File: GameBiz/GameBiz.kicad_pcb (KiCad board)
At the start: 2 copper layers, 89 x 51 mm, 90 parts, among them J1 USB4155-03-C_REVA, M1 C0720B001F, Q1 PMCXB900UEZ, SW1 CUS-12TB, U1 W25Q128JV, U2 RP2040, U3 NCV8718BMT330TBG, U4 BQ25172DSGR, U5 74LVC1G3157FZ4-7, U6 NRF24L01, U7 IQS7222A001QNR, U8 TPS61291DRVT, U9 EADOGS104NA, Y1 12MHz, Y2 ECS-160-18-30B-JEM-TR

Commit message: layout almost finished
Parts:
- removed TH1: Thermistor, Resistor_SMD:R_0603_1608Metric
- added R12: 10K, Resistor_SMD:R_0603_1608Metric, F.Cu at (159.9, 139.8)
- moved C19 118.0 mm to (131.4, 141.5)
- moved R21 117.4 mm to (176.4, 144.1), turned to -90 degrees
- moved Y2 116.0 mm to (179.2, 142.7), turned to -90 degrees
- moved SW1 115.4 mm to (140.8, 152.1)
- moved R13 115.2 mm to (118.2, 150.3)
- moved L3 115.2 mm to (191.9, 144.4), turned to -90 degrees
- moved D3 114.7 mm to (161.5, 141.6), turned to -90 degrees
- moved U4 109.8 mm to (157.7, 139.8), turned to 90 degrees
- moved U3 108.3 mm to (158.2, 144.9), turned to -90 degrees
- moved C15 107.3 mm to (156.4, 143.0), turned to -90 degrees
- moved R7 106.3 mm to (158.8, 142.2)
- moved U6 105.8 mm to (183.9, 142.4)
- moved R16 105.6 mm to (111.9, 143.0)
- moved C10 105.0 mm to (151.9, 128.1), turned to -90 degrees
- moved D2 104.7 mm to (145.0, 136.1), turned to -90 degrees
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- renumbered R12 to R13, R13 to R14, R14 to R15, R15 to R16, R16 to R17, R17 to R18, R18 to R19, R19 to R20, R20 to R21
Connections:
- AE1 pad 1: GND -> Net-(AE1-Pad2)
- AE1 pad 2: Net-(AE1-Pad2) -> GND
- D2 pad 1: unconnected-(D2-Pad1) -> Net-(D1-Pad1)
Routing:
- net Net-(BT1-Pad2): track 0.00 -> 180.5 mm, vias 0 -> 1
- net +3.3V: track 0.00 -> 94.4 mm
- net GND: track 0.00 -> 66.3 mm
- net Net-(C13-Pad2): track 0.00 -> 31.8 mm
- net Net-(C12-Pad2): track 0.00 -> 26.4 mm
- net Net-(BT1-Pad1): track 0.00 -> 26.1 mm, vias 0 -> 2
- net Net-(SW1-Pad2): track 0.00 -> 25.9 mm
- net Net-(J1-PadA6): track 0.00 -> 25.0 mm, vias 0 -> 2
- net Net-(R3-Pad1): track 0.00 -> 24.8 mm
- net Net-(C22-Pad2): track 0.00 -> 20.9 mm
- net Net-(Q1-Pad2): track 0.00 -> 19.9 mm
- net Net-(U1-Pad7): track 0.00 -> 19.5 mm
- net Net-(U1-Pad6): track 0.00 -> 17.2 mm
- net Net-(J1-PadA7): track 0.00 -> 16.6 mm, vias 0 -> 2
- net Net-(U1-Pad5): track 0.00 -> 14.0 mm
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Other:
- outline, holes or cut-outs redrawn

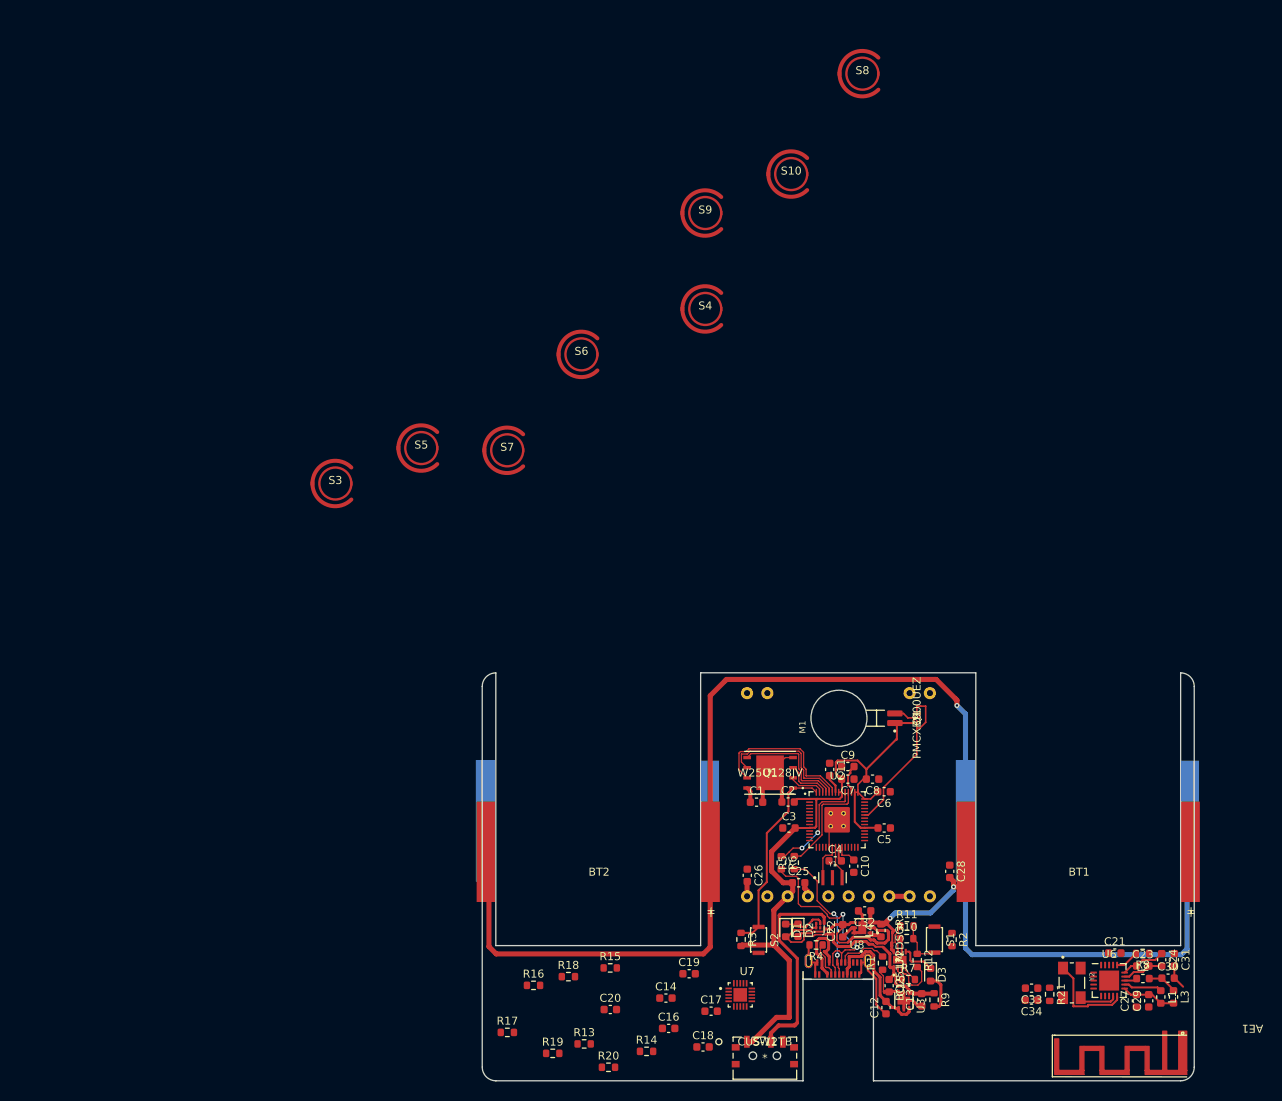
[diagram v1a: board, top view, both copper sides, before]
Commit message: capacitive buttons need to be finished
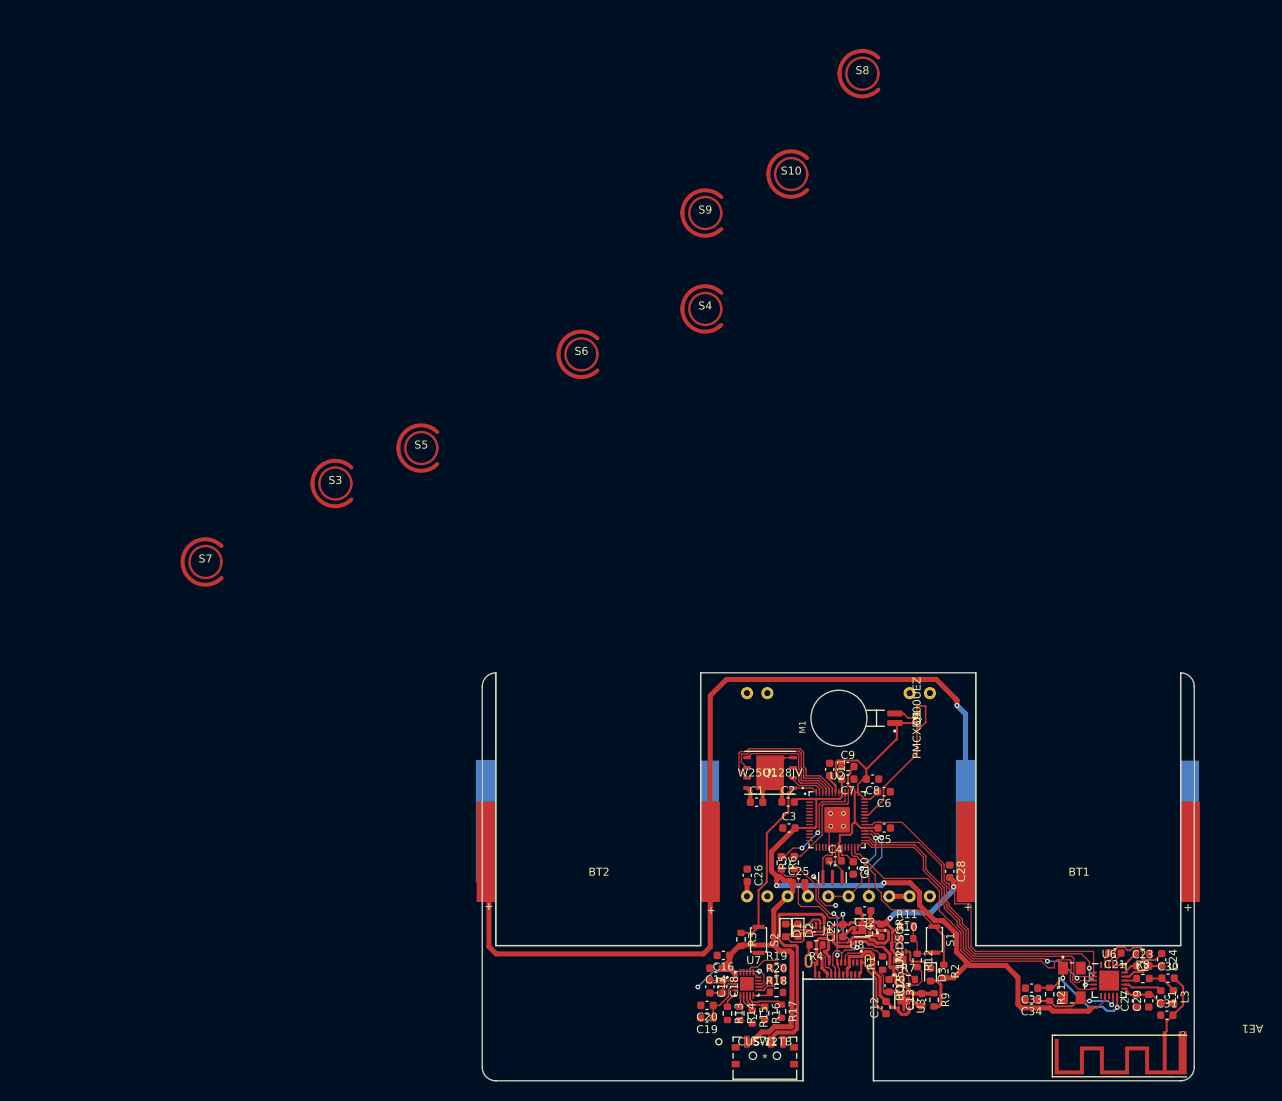
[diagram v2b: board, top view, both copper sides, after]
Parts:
- moved S7 40.2 mm to (70.9, 90.0)
- moved R17 34.4 mm to (142.9, 146.2), turned to -90 degrees
- moved R19 30.0 mm to (142.3, 140.7)
- moved R16 29.1 mm to (140.8, 146.4), turned to -90 degrees
- moved R18 26.1 mm to (142.3, 143.8)
- moved R20 23.7 mm to (142.3, 142.3)
- moved R15 18.8 mm to (139.2, 146.9), turned to -90 degrees
- moved R13 18.3 mm to (136.2, 146.5), turned to -90 degrees
- moved R14 12.6 mm to (137.7, 146.5), turned to -90 degrees
- moved C20 12.1 mm to (133.6, 145.5), turned to 180 degrees
- moved C16 11.4 mm to (135.7, 139.2), turned to 180 degrees
- moved C18 7.91 mm to (135.6, 143.2), turned to -90 degrees
- moved C14 7.27 mm to (134.7, 140.8), turned to 180 degrees
- moved C31 6.99 mm to (191.1, 146.7), turned to 0 degrees
- moved C19 5.97 mm to (133.6, 147.1), turned to 180 degrees
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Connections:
- AE1 pad 2: GND -> Net-(AE1-Pad2)
- U6 pad 4: Net-(U2-Pad27) -> Net-(U2-Pad30)
- U6 pad 5: Net-(U2-Pad30) -> Net-(U2-Pad27)
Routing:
- net +3.3V: track 94.4 -> 172.7 mm, vias 0 -> 2
- net Net-(BT1-Pad2): track 180.5 -> 120.1 mm
- net Net-(U2-Pad34): track 0.00 -> 44.4 mm
- net Net-(U2-Pad27): track 0.00 -> 43.3 mm
- net Net-(U2-Pad30): track 0.00 -> 42.8 mm, vias 0 -> 2
- net Net-(U2-Pad29): track 0.00 -> 41.7 mm
- net Net-(U2-Pad28): track 0.00 -> 40.6 mm, vias 0 -> 2
- net Net-(R2-Pad1): track 0.00 -> 21.6 mm
- net Net-(U2-Pad31): track 0.00 -> 12.8 mm, vias 0 -> 2
- net Net-(S10-Pad1): track 0.00 -> 10.9 mm, vias 0 -> 2
- net Net-(U2-Pad32): track 0.00 -> 10.7 mm, vias 0 -> 2
- net GND: track 66.3 -> 73.2 mm, vias 0 -> 2
- net Net-(C34-Pad1): track 4.78 -> 11.5 mm, vias 0 -> 2
- net Net-(C19-Pad1): track 0.00 -> 5.75 mm
- net (no net): track 0.00 -> 5.51 mm
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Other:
- outline, holes or cut-outs redrawn

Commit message: Update GameBiz.kicad_pcb
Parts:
- moved S8 122.8 mm to (172.6, 150.2)
- moved S10 112.9 mm to (166.3, 152.3)
- moved S9 104.5 mm to (166.4, 145.5)
- moved S4 95.7 mm to (159.9, 150.4)
- moved S6 87.5 mm to (118.0, 151.6)
- moved S7 78.9 mm to (123.9, 148.6)
- moved S3 73.3 mm to (112.1, 149.1)
- moved S5 70.8 mm to (117.9, 143.8)
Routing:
- net GND: track 73.2 -> 115.5 mm, vias 2 -> 10
- net Net-(R18-Pad2): track 0.00 -> 27.0 mm, vias 0 -> 2
- net Net-(R20-Pad2): track 0.00 -> 23.1 mm, vias 0 -> 2
- net Net-(R19-Pad2): track 0.00 -> 21.2 mm, vias 0 -> 2
- net Net-(C10-Pad1): track 8.83 -> 29.0 mm, vias 0 -> 4
- net Net-(S10-Pad1): track 10.9 -> 23.8 mm
- net Net-(R16-Pad2): track 0.00 -> 11.7 mm
- net Net-(R15-Pad2): track 0.00 -> 10.1 mm
- net Net-(R14-Pad2): track 0.00 -> 8.90 mm
- net Net-(R13-Pad2): track 0.00 -> 7.52 mm
- net +3.3V: track 172.7 -> 172.0 mm

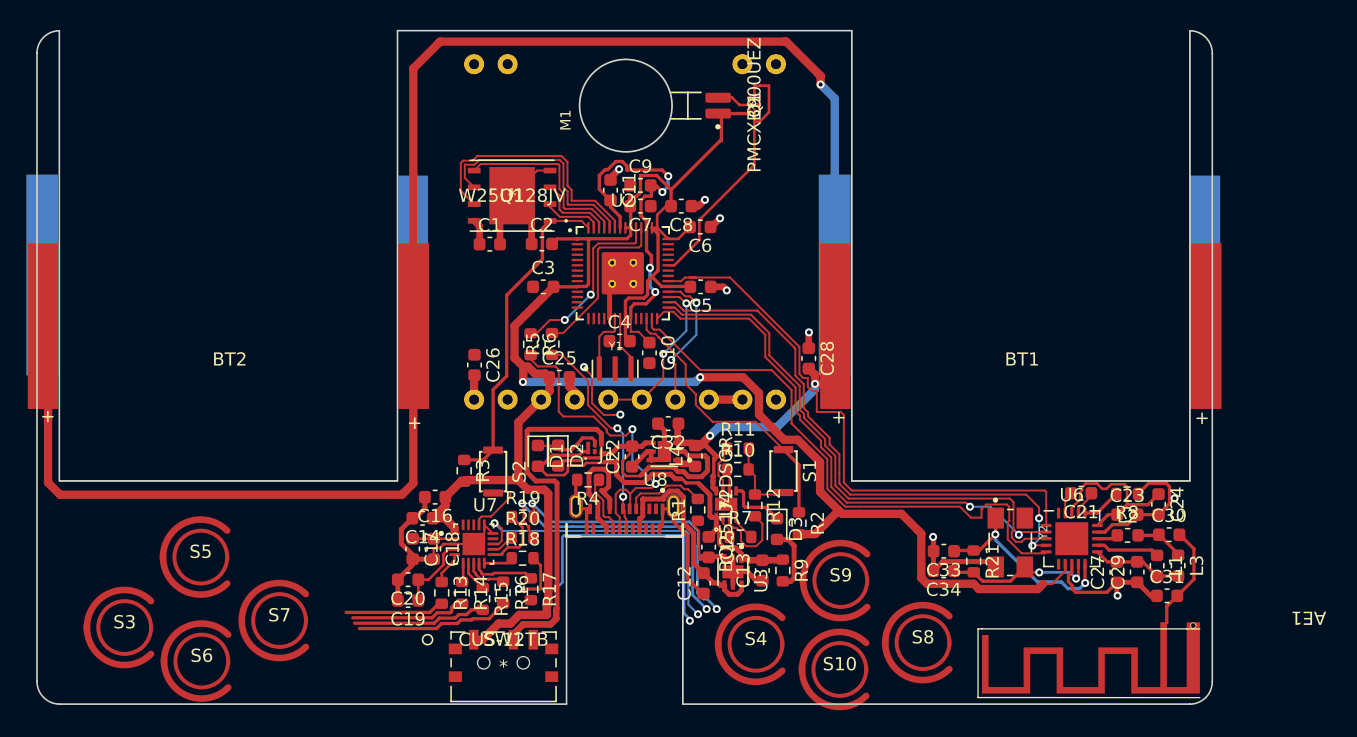
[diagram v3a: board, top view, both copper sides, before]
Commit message: finished initial layout, still some errors
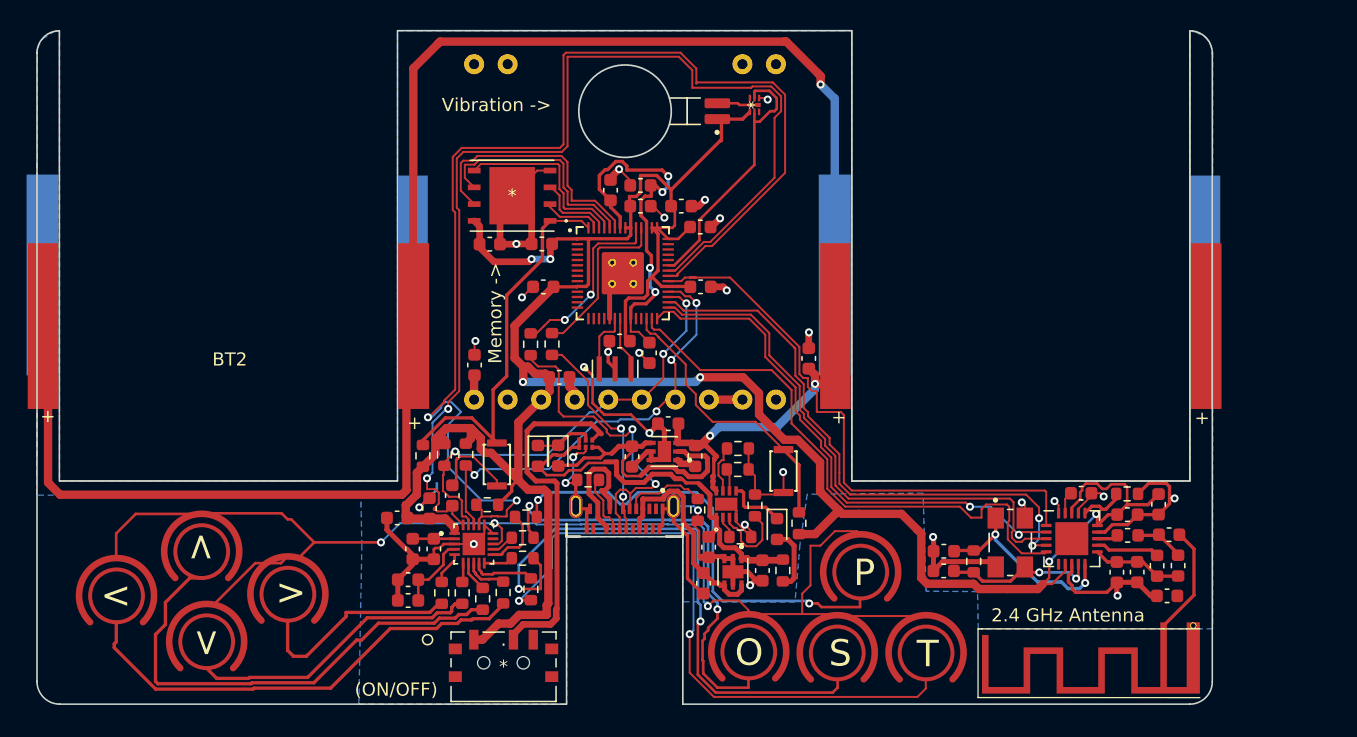
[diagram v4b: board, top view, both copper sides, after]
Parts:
- added C19: 100nF, Capacitor_SMD:C_0603_1608Metric, F.Cu at (136.9, 139.1)
- added R11: 4.7K, Resistor_SMD:R_0603_1608Metric, F.Cu at (138.0, 136.0)
- added R12: 4.7K, Resistor_SMD:R_0603_1608Metric, F.Cu at (136.3, 136.0)
- added R8: 4.7K, Resistor_SMD:R_0603_1608Metric, F.Cu at (139.6, 139.8)
- (ON/OFF): renamed from SW1; value CUS-12TB -> .
- 2.4 GHz Antenna: renamed from AE1
- Q1: value PMCXB900UEZ -> Vibration ->
- U1: value W25Q128JV -> Memory ->
- moved R3 3.32 mm to (134.7, 136.1)
- moved < 2.48 mm to (111.5, 146.7), turned to -90 degrees
- moved > 2.09 mm to (124.5, 146.6), turned to -90 degrees
- moved C14 1.93 mm to (132.8, 140.8)
- moved P 1.64 mm to (167.9, 144.9), turned to -90 degrees
- moved > 1.51 mm to (118.3, 150.2), turned to -90 degrees
- moved S 1.26 mm to (166.1, 151.0), turned to -90 degrees
- moved C16 0.95 mm to (135.2, 140.1), turned to 90 degrees
- moved T 0.82 mm to (172.8, 151.0), turned to -90 degrees
- moved O 0.80 mm to (159.4, 150.9), turned to -90 degrees
- moved U5 0.76 mm to (147.1, 135.2)
- moved S2 0.61 mm to (140.3, 136.8)
- moved M1 0.42 mm to (152.0, 110.0)
- moved > 0.42 mm to (118.0, 143.3), turned to -90 degrees
- moved R22 0.22 mm to (142.5, 140.7)
- renumbered S3 to <, S6 to >, S5 to >, S7 to >, C19 to C20, C20 to C21, C21 to C22, C22 to C23, C23 to C24, C24 to C25, C25 to C26, C26 to C27, C27 to C28, C28 to C29, C29 to C30, C30 to C31, C31 to C32, C32 to C33, C33 to C34, C34 to C35, S4 to O, S9 to P, R9 to R10, R10 to R13, R11 to R14, R12 to R15, R13 to R16, R14 to R17, R15 to R18, R16 to R19, R17 to R20, R18 to R21, R19 to R22, R20 to R23, R21 to R24, R8 to R9, S10 to S, S8 to T
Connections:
- < pad Rx: (no net) -> Net-(R19-Pad2)
- < pad Tx: (no net) -> Net-(S10-Pad1)
- > pad Rx: (no net) -> Net-(R17-Pad2)
- > pad Tx: (no net) -> Net-(S10-Pad1) (x3)
- > pad Rx: (no net) -> Net-(R18-Pad2)
- > pad Rx: (no net) -> Net-(R16-Pad2)
- O pad Rx: (no net) -> Net-(R23-Pad2)
- O pad Tx: (no net) -> Net-(S10-Pad1)
- P pad Rx: (no net) -> Net-(R22-Pad2)
- P pad Tx: (no net) -> Net-(S10-Pad1)
- R16 pad 2: Net-(R13-Pad2) -> Net-(R16-Pad2)
- R17 pad 2: Net-(R14-Pad2) -> Net-(R17-Pad2)
- R18 pad 2: Net-(R15-Pad2) (its old number) -> Net-(R18-Pad2)
- R19 pad 2: Net-(R16-Pad2) -> Net-(R19-Pad2)
- R20 pad 2: Net-(R17-Pad2) -> Net-(R20-Pad2)
- R21 pad 2: Net-(R18-Pad2) -> Net-(R21-Pad2)
- R22 pad 2: Net-(R19-Pad2) -> Net-(R22-Pad2)
- R23 pad 2: Net-(R20-Pad2) -> Net-(R23-Pad2)
- S pad Rx: (no net) -> Net-(R21-Pad2)
- S pad Tx: (no net) -> Net-(S10-Pad1)
- T pad Rx: (no net) -> Net-(R20-Pad2)
- T pad Tx: (no net) -> Net-(S10-Pad1)
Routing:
- net Net-(R8-Pad2): track 3.92 -> 92.8 mm, vias 0 -> 2
- net Net-(C19-Pad1): track 0.00 -> 83.2 mm, vias 0 -> 2
- net Net-(S10-Pad1): track 23.8 -> 93.9 mm, vias 2 -> 3
- net Net-(R21-Pad2): track 0.00 -> 43.8 mm, vias 0 -> 2
- net GND: track 115.5 -> 159.0 mm, vias 10 -> 28
- net Net-(R22-Pad2): track 0.00 -> 34.6 mm, vias 0 -> 2
- net Net-(R23-Pad2): track 0.00 -> 33.5 mm, vias 0 -> 2
- net +3.3V: track 172.0 -> 202.0 mm, vias 2 -> 6
- net Net-(R20-Pad2): track 23.1 -> 47.9 mm
- net Net-(R11-Pad2): track 10.7 -> 34.1 mm, vias 2 -> 4
- net Net-(R17-Pad2): track 0.00 -> 22.2 mm
- net Net-(R12-Pad1): track 12.8 -> 33.5 mm, vias 2 -> 3
- net Net-(R19-Pad2): track 21.2 -> 35.5 mm, vias 2 -> 0
- net Net-(R15-Pad2) (its old number): track 10.1 -> 0.00 mm
- net Net-(R18-Pad2): track 27.0 -> 37.0 mm, vias 2 -> 0
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- added copper zone on B.Cu, net GND

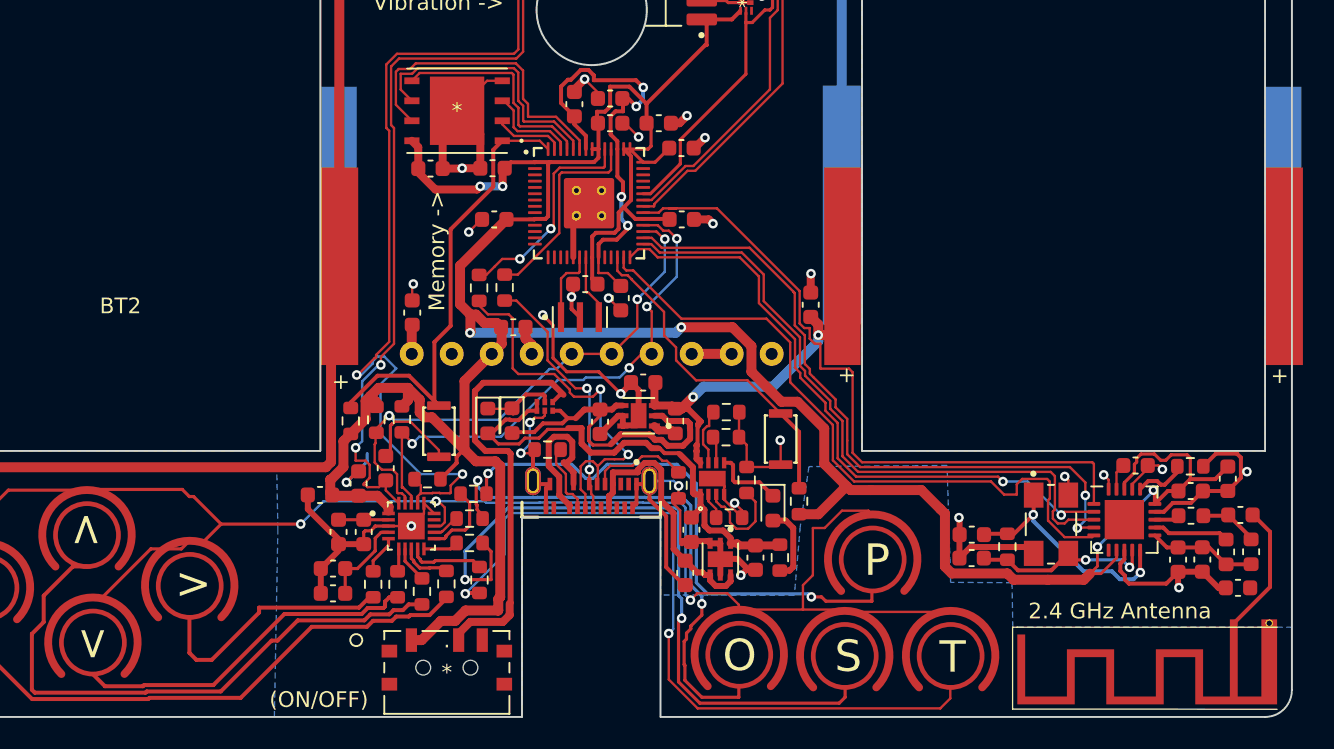
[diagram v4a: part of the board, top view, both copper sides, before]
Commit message: fixed most errors
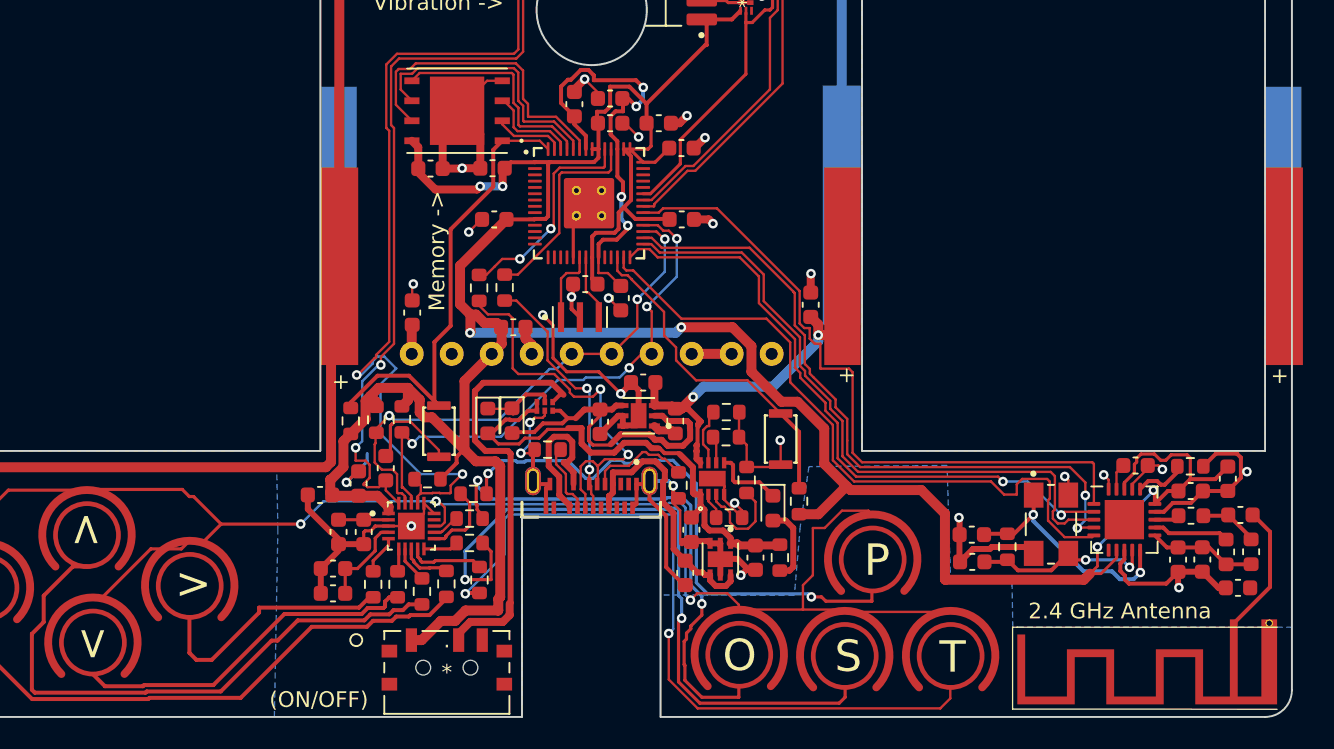
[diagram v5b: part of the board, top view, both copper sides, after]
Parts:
- moved C35 0.24 mm to (174.2, 145.1)
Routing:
- net Net-(U2-Pad34): track 44.4 -> 43.5 mm
- net Net-(R22-Pad2): track 34.6 -> 35.3 mm
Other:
- board text added: "Designed by Phillip Post & Jacob Prisament"
